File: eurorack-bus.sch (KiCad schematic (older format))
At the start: 5 parts, among them J1 Conn_02x08_Odd_Even, J3 Conn_02x08_Odd_Even, J4 Conn_02x08_Odd_Even, J5 Conn_02x08_Odd_Even, J6 Conn_02x08_Odd_Even

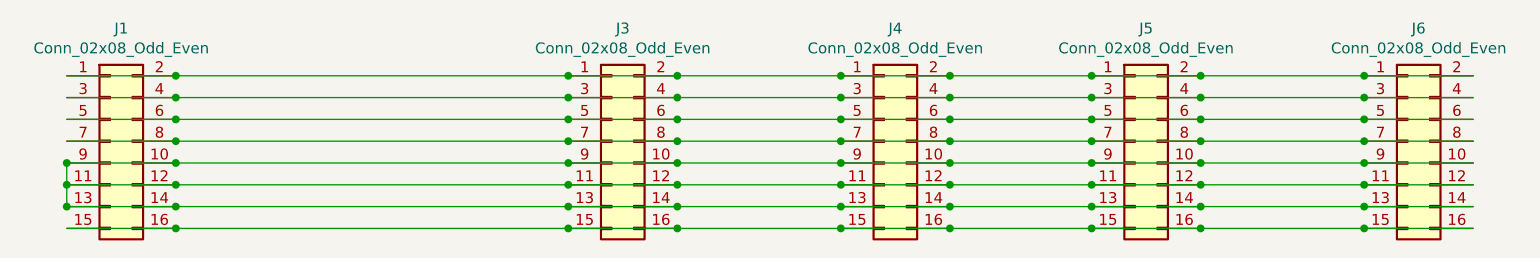
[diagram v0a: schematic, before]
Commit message: readd conn J2, rm 5v/cv/gt tracks, route
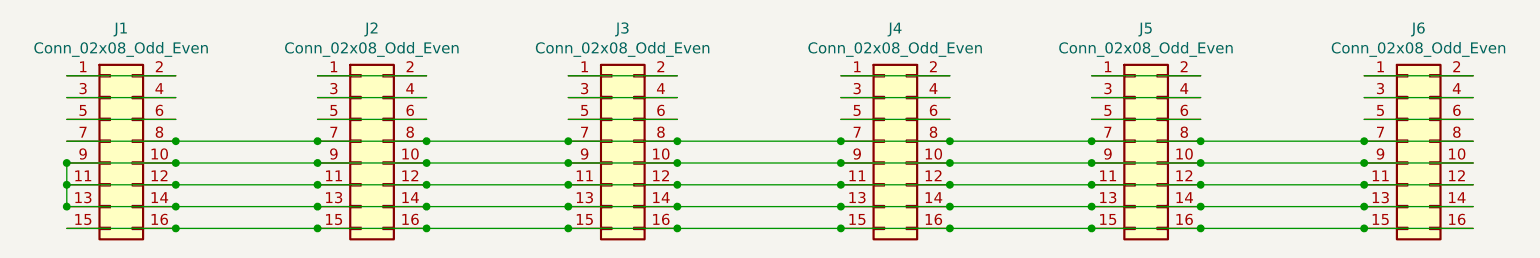
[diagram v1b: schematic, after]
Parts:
- added J2: Conn_02x08_Odd_Even, Connector_PinSocket_2.54mm:PinSocket_2x08_P2.54mm_Vertical, symbol Connector_Generic:Conn_02x08_Odd_Even
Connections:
- net at J1.10 (Pin_10), J1.11 (Pin_11), J1.12 (Pin_12)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: now also J2.10 (Pin_10), J2.11 (Pin_11), J2.12 (Pin_12), J2.13 (Pin_13), J2.14 (Pin_14), J2.9 (Pin_9)
- net at J1.15 (Pin_15), J1.16 (Pin_16), J3.15 (Pin_15)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: now also J2.15 (Pin_15), J2.16 (Pin_16)
- net at J1.7 (Pin_7), J1.8 (Pin_8), J3.7 (Pin_7)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: now also J2.7 (Pin_7), J2.8 (Pin_8)
- new net: J4.1 (Pin_1), J4.2 (Pin_2)
- new net: J4.3 (Pin_3), J4.4 (Pin_4)
- new net: J4.5 (Pin_5), J4.6 (Pin_6)
- new net: J3.1 (Pin_1), J3.2 (Pin_2)
- new net: J3.3 (Pin_3), J3.4 (Pin_4)
- new net: J3.5 (Pin_5), J3.6 (Pin_6)
- new net: J2.1 (Pin_1), J2.2 (Pin_2)
- new net: J2.3 (Pin_3), J2.4 (Pin_4)
- new net: J2.5 (Pin_5), J2.6 (Pin_6)
- new net: J1.1 (Pin_1), J1.2 (Pin_2)
- new net: J1.3 (Pin_3), J1.4 (Pin_4)
- new net: J1.5 (Pin_5), J1.6 (Pin_6)
- new net: J5.1 (Pin_1), J5.2 (Pin_2)
- new net: J5.3 (Pin_3), J5.4 (Pin_4)
- new net: J5.5 (Pin_5), J5.6 (Pin_6)
- new net: J6.1 (Pin_1), J6.2 (Pin_2)
- new net: J6.3 (Pin_3), J6.4 (Pin_4)
- new net: J6.5 (Pin_5), J6.6 (Pin_6)
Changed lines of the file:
@@
 Wire Wire Line
 	1300 2550 1800 2550
-Connection ~ 1800 2550
 Wire Wire Line
 	1300 2650 1800 2650
-Connection ~ 1800 2650
 Wire Wire Line
 	1300 2750 1800 2750
-Connection ~ 1800 2750
 Wire Wire Line
 	1300 2850 1800 2850
@@
 Wire Wire Line
 	3600 2550 4100 2550
-Connection ~ 3600 2550
 Wire Wire Line
 	4100 2650 3600 2650
-Connection ~ 3600 2650
 Wire Wire Line
 	3600 2750 4100 2750
-Connection ~ 3600 2750
 Wire Wire Line
 	4100 2850 3600 2850
@@
 Connection ~ 4100 2950
 Connection ~ 4100 2850
-Connection ~ 4100 2750
-Connection ~ 4100 2650
 Connection ~ 4100 3250
 Connection ~ 4100 3150
 Connection ~ 4100 3050
-Connection ~ 4100 2550
 Wire Wire Line
 	5350 2950 4850 2950
@@
 	5350 2750 4850 2750
 Wire Wire Line
-	4100 2750 4850 2750
-Connection ~ 4850 2750
-Wire Wire Line
 	4850 2650 5350 2650
-Wire Wire Line
-	4850 2650 4100 2650
-Connection ~ 4850 2650
 Wire Wire Line
 	4850 3250 5350 3250
@@
 Wire Wire Line
 	5350 2550 4850 2550
-Wire Wire Line
-	4100 2550 4850 2550
-Connection ~ 4850 2550
 $Comp
 L Connector_Generic:Conn_02x08_Odd_Even J4
@@
 $EndComp
 Wire Wire Line
-	5350 2550 6000 2550
-Wire Wire Line
-	6000 2650 5350 2650
-Wire Wire Line
-	5350 2750 6000 2750
-Wire Wire Line
 	6000 2850 5350 2850
 Wire Wire Line
@@
 Wire Wire Line
 	6000 2550 6500 2550
-Connection ~ 6000 2550
 Wire Wire Line
 	6500 2650 6000 2650
-Connection ~ 6000 2650
 Wire Wire Line
 	6000 2750 6500 2750
-Connection ~ 6000 2750
 Wire Wire Line
 	6500 2850 6000 2850
@@
 Connection ~ 6500 2950
 Connection ~ 6500 2850
-Connection ~ 6500 2750
-Connection ~ 6500 2650
 Connection ~ 6500 3250
 Connection ~ 6500 3150
 Connection ~ 6500 3050
-Connection ~ 6500 2550
 Wire Wire Line
 	7750 2950 7250 2950
@@
 	7750 2750 7250 2750
 Wire Wire Line
-	6500 2750 7250 2750
-Connection ~ 7250 2750
-Wire Wire Line
 	7250 2650 7750 2650
-Wire Wire Line
-	7250 2650 6500 2650
-Connection ~ 7250 2650
 Wire Wire Line
 	7250 3250 7750 3250
@@
 Wire Wire Line
 	7750 2550 7250 2550
-Wire Wire Line
-	6500 2550 7250 2550
-Connection ~ 7250 2550
 $Comp
 L Connector_Generic:Conn_02x08_Odd_Even J6
@@
 	1    0    0    -1
 $EndComp
-Connection ~ 5350 2550
-Connection ~ 5350 2650
-Connection ~ 5350 2750
 Connection ~ 5350 2850
 Connection ~ 5350 2950
@@
 Connection ~ 1300 2950
 Wire Wire Line
-	1800 3050 3600 3050
-Wire Wire Line
-	1800 3150 3600 3150
-Wire Wire Line
-	1800 3250 3600 3250
-Wire Wire Line
-	1800 2550 3600 2550
-Wire Wire Line
-	1800 2650 3600 2650
-Wire Wire Line
-	1800 2750 3600 2750
-Wire Wire Line
-	1800 2850 3600 2850
-Wire Wire Line
-	1800 2950 3600 2950
+	1800 2950 2450 2950
+Connection ~ 2450 2950
+Wire Wire Line
+	3600 2850 2950 2850
+Connection ~ 2950 2850
+Wire Wire Line
+	2950 2850 2450 2850
+Wire Wire Line
+	1800 2850 2450 2850
+Connection ~ 2450 2850
+Wire Wire Line
+	2450 2750 2950 2750
+Wire Wire Line
+	2450 2650 2950 2650
+Wire Wire Line
+	2950 3250 3600 3250
+Connection ~ 2950 3250
+Wire Wire Line
+	2950 3250 2450 3250
+Wire Wire Line
+	1800 3250 2450 3250
+Connection ~ 2450 3250
+Wire Wire Line
+	2950 3150 3600 3150
+Connection ~ 2950 3150
+Wire Wire Line
+	2450 3150 2950 3150
+Wire Wire Line
+	1800 3150 2450 3150
+Connection ~ 2450 3150
+Wire Wire Line
+	2950 3050 3600 3050
+Connection ~ 2950 3050
+Wire Wire Line
+	2950 3050 2450 3050
+Wire Wire Line
+	1800 3050 2450 3050
+Connection ~ 2450 3050
+Wire Wire Line
+	2450 2950 2950 2950
+Wire Wire Line
+	2950 2950 3600 2950
+Connection ~ 2950 2950
+Wire Wire Line
+	2450 2550 2950 2550
+$Comp
+L Connector_Generic:Conn_02x08_Odd_Even J2
+U 1 1 5CC2B337
+P 2650 2850
+F 0 "J2" H 2700 3367 50  0000 C CNN
+F 1 "Conn_02x08_Odd_Even" H 2700 3276 50  0000 C CNN
+F 2 "Connector_PinSocket_2.54mm:PinSocket_2x08_P2.54mm_Vertical" H 2650 2850 50  0001 C CNN
+F 3 "~" H 2650 2850 50  0001 C CNN
+	1    2650 2850
+	1    0    0    -1
+$EndComp
 $EndSCHEMATC

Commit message: add traces for 5v line throughout
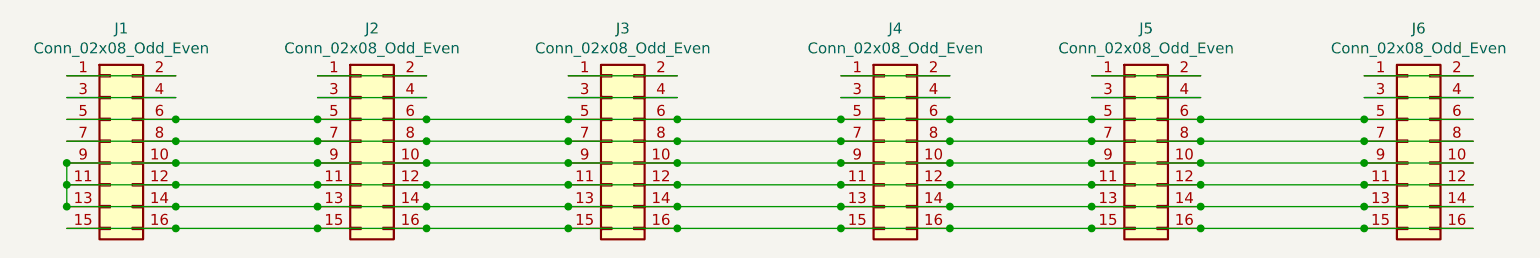
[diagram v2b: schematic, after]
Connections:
- net at J4.5 (Pin_5), J4.6 (Pin_6): now also J1.5 (Pin_5), J1.6 (Pin_6), J2.5 (Pin_5), J2.6 (Pin_6), J3.5 (Pin_5), J3.6 (Pin_6), J5.5 (Pin_5), J5.6 (Pin_6), J6.5 (Pin_5), J6.6 (Pin_6)
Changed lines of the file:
@@
 	4100 2650 3600 2650
-Wire Wire Line
-	3600 2750 4100 2750
 Wire Wire Line
 	4100 2850 3600 2850
@@
 Connection ~ 2450 2850
 Wire Wire Line
-	2450 2750 2950 2750
-Wire Wire Line
 	2450 2650 2950 2650
 Wire Wire Line
@@
 	1    0    0    -1
 $EndComp
+Wire Wire Line
+	1800 2750 2450 2750
+Connection ~ 1800 2750
+Connection ~ 2450 2750
+Wire Wire Line
+	2450 2750 2950 2750
+Wire Wire Line
+	2950 2750 3600 2750
+Connection ~ 2950 2750
+Connection ~ 3600 2750
+Wire Wire Line
+	3600 2750 4100 2750
+Wire Wire Line
+	4100 2750 4850 2750
+Connection ~ 4100 2750
+Connection ~ 4850 2750
+Wire Wire Line
+	5350 2750 6000 2750
+Connection ~ 5350 2750
+Connection ~ 6000 2750
+Wire Wire Line
+	6500 2750 7250 2750
+Connection ~ 6500 2750
+Connection ~ 7250 2750
 $EndSCHEMATC
